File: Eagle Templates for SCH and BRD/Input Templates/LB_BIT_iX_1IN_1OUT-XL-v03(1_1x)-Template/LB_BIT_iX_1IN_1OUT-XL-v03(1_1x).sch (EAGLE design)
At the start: 16 parts, among them U1 LV321SOT23-5, U2 LV321SOT23-5

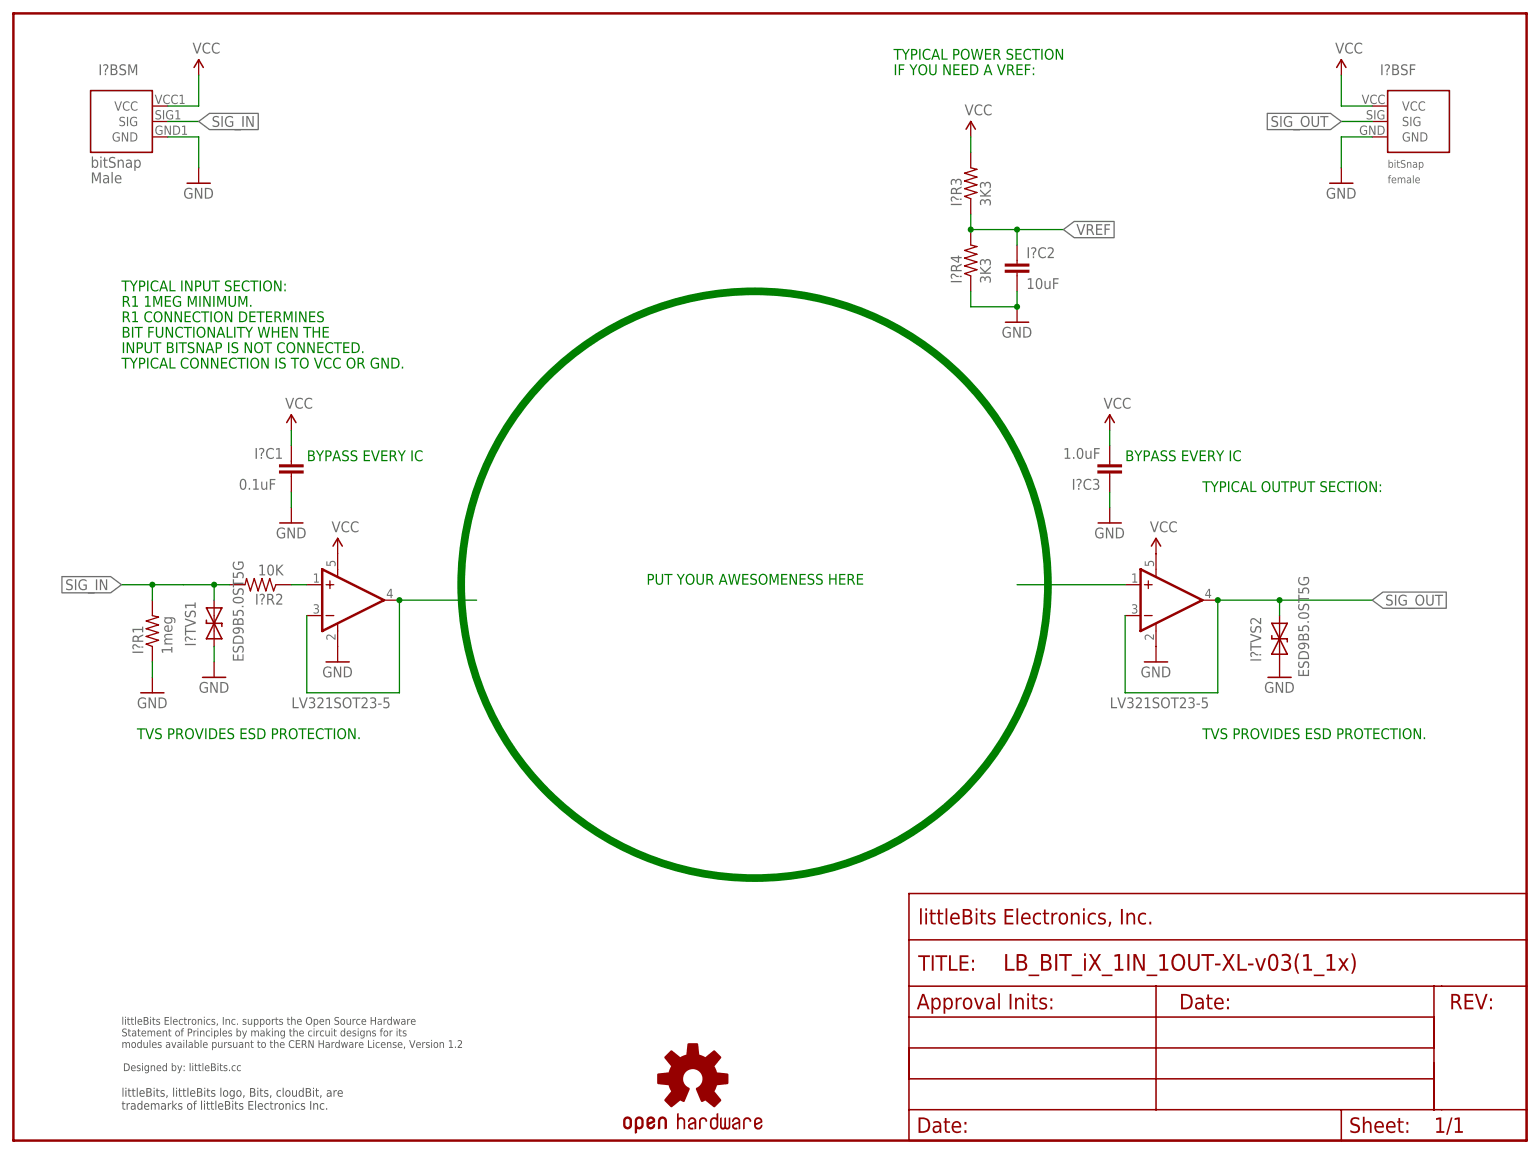
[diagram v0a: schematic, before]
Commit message: Updated templates
- Added ferrite beads
- Moved text and annotations off of Nets layer
- Minor layout changes
- Removed I/O/W prefix from reference designators
- Removed output stage components from output bits
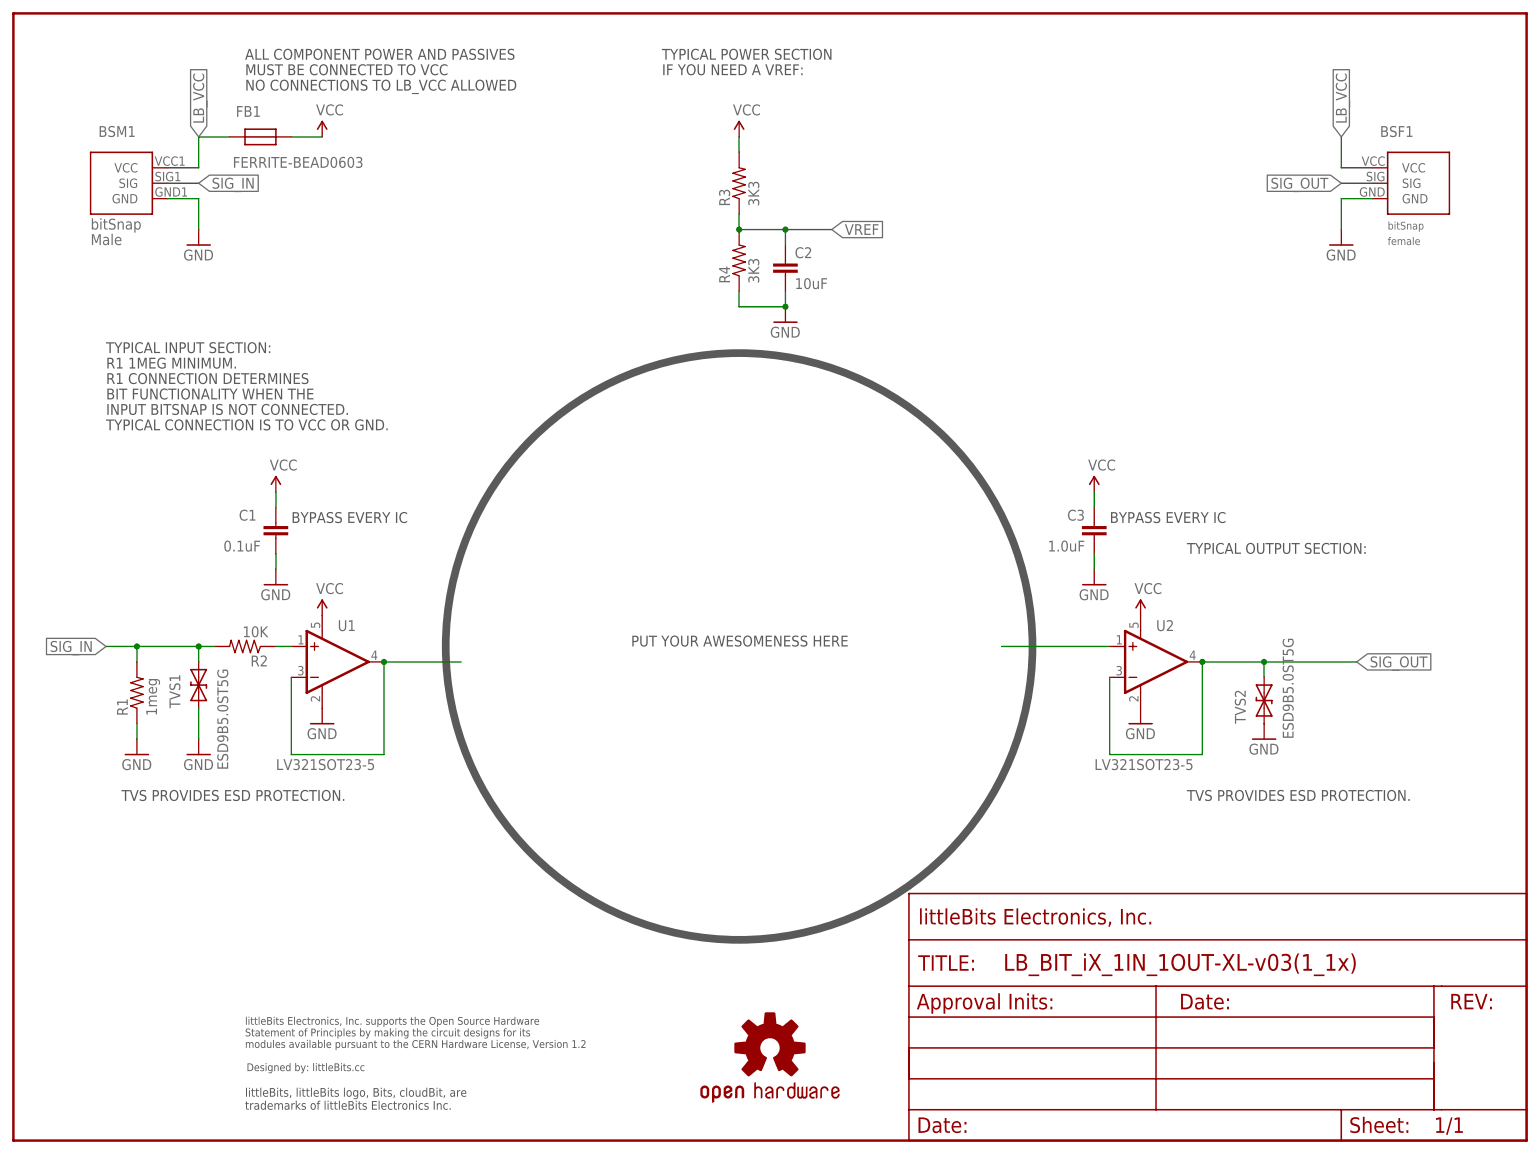
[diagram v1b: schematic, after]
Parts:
- removed I?BSF: BITSNAP_V03_FEMALE, bitSnap:BITSNAP_V03_FEMALE
- removed I?BSM: BITSNAP_V03_MALE, bitSnap:BITSNAP_V03_MALE
- removed I?C1: 0.1uF, LITTLEBITS:CAPCAP-0603
- removed I?C2: 10uF, LITTLEBITS:CAPCAP-0603
- removed I?C3: 1.0uF, LITTLEBITS:CAPCAP-0603
- removed I?R1: 1meg, LITTLEBITS:RESISTOR0603
- removed I?R2: 10K, LITTLEBITS:RESISTOR0603
- removed I?R3, I?R4: 3K3, LITTLEBITS:RESISTOR0603
- removed I?TVS1, I?TVS2: ESD9B5.0ST5G, LITTLEBITS:DIODE-TVSSOD-923
- added BSF1: BITSNAP_V03_FEMALE, bitSnap:BITSNAP_V03_FEMALE
- added BSM1: BITSNAP_V03_MALE, bitSnap:BITSNAP_V03_MALE
- added C1: 0.1uF, LITTLEBITS:CAPCAP-0603
- added C2: 10uF, LITTLEBITS:CAPCAP-0603
- added C3: 1.0uF, LITTLEBITS:CAPCAP-0603
- added FB1: FERRITE-BEAD0603, LITTLEBITS:FERRITE-BEAD0603
- added R1: 1meg, LITTLEBITS:RESISTOR0603
- added R2: 10K, LITTLEBITS:RESISTOR0603
- added R3, R4: 3K3, LITTLEBITS:RESISTOR0603
- added TVS1, TVS2: ESD9B5.0ST5G, LITTLEBITS:DIODE-TVSSOD-923
- U$2: value FRAME-LETTER -> OSHWCREDIT; device LITTLEBITS:FRAME-LETTER -> LITTLEBITS:OSHWCREDIT
- U$3: value OSHWCREDIT -> FRAME-LETTER; device LITTLEBITS:OSHWCREDIT -> LITTLEBITS:FRAME-LETTER
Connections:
- removed net N1: I?BSF.GND, I?BSM.GND
- new net LB_VCC: BSF1.VCC, BSM1.VCC, FB1.P$2
- net GND: now also BSF1.GND, BSM1.GND, C1.2, C2.2, C3.1, R1.1, R4.1, TVS1.A, TVS2.A; no longer I?C1.2, I?C2.2, I?C3.1, I?R1.1, I?R4.1, I?TVS1.A, I?TVS2.A
- net N$4: now also R2.1; no longer I?R2.1
- net SIG_IN: now also BSM1.SIG, R1.2, R2.2, TVS1.C; no longer I?BSM.SIG, I?R1.2, I?R2.2, I?TVS1.C
- net SIG_OUT: now also BSF1.SIG, TVS2.C; no longer I?BSF.SIG, I?TVS2.C
- net VCC: now also C1.1, C3.2, FB1.P$1, R3.2; no longer I?BSF.VCC, I?BSM.VCC, I?C1.1, I?C3.2, I?R3.2
- net VREF: now also C2.1, R3.1, R4.2; no longer I?C2.1, I?R3.1, I?R4.2
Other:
- note added: "ALL COMPONENT POWER AND PASSIVES"
- note added: "MUST BE CONNECTED TO VCC"
- note added: "NO CONNECTIONS TO LB_VCC ALLOWED"
